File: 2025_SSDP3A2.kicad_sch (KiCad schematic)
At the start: 62 parts, among them J1 SolderPad, J2 SolderPad, J3 SolderPad, J4 SolderPad, J5 SolderPad_01x06, Q1 IAUZ30N10S5L240, Q2 BSZ096N10LS5, U1 LM5146RGYR

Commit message: Tweaks in schematic and layout
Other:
- note added: "V_{IN} = 20~60V (70V transient) typ. 6~12S Li-Ion/LiPo Battery"
- note removed: "V_{IN} = 20~70V (50V Nom) typ. 6~12S Li-Ion/LiPo Battery"
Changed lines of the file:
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@@
 		)
 	)
-	(text "V_{IN} = 20~70V (50V Nom)\ntyp. 6~12S Li-Ion/LiPo Battery"
+	(text "V_{IN} = 20~60V (70V transient)\ntyp. 6~12S Li-Ion/LiPo Battery"
 		(exclude_from_sim no)
 		(at 315.976 98.044 0)

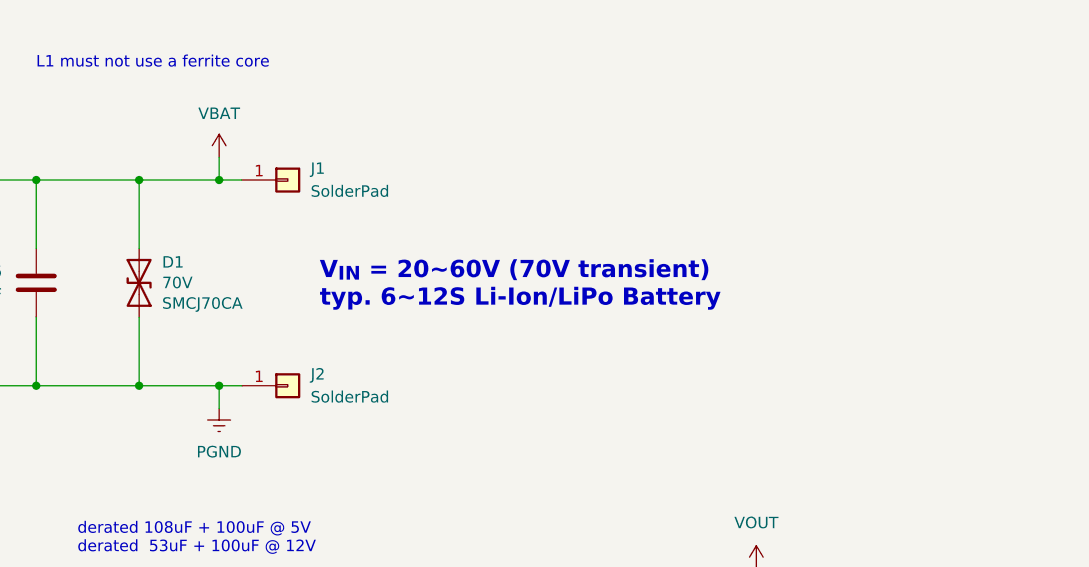
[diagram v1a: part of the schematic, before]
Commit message: Changed TVS diode
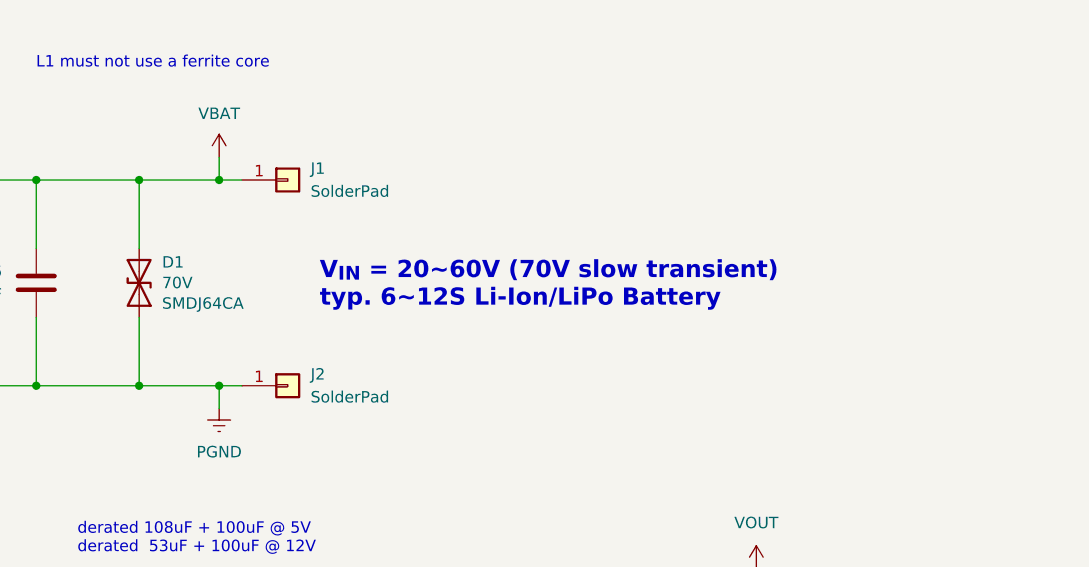
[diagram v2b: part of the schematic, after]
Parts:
- D1: LCSC PN C41411746 -> C42371551; Power (none) -> 3000W; Voltage 113V -> 103V
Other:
- note added: "V_{IN} = 20~60V (70V slow transient) typ. 6~12S Li-Ion/LiPo Battery"
- note removed: "V_{IN} = 20~60V (70V transient) typ. 6~12S Li-Ion/LiPo Battery"
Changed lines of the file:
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@@
 		)
 	)
-	(text "V_{IN} = 20~60V (70V transient)\ntyp. 6~12S Li-Ion/LiPo Battery"
+	(text "V_{IN} = 20~60V (70V slow transient)\ntyp. 6~12S Li-Ion/LiPo Battery"
 		(exclude_from_sim no)
 		(at 315.976 98.044 0)
@@
 			)
 		)
-		(property "Datasheet" "https://jlcpcb.com/api/file/downloadByFileSystemAccessId/8604441788598415360"
+		(property "Datasheet" "https://jlcpcb.com/api/file/downloadByFileSystemAccessId/8564879186138451968"
 			(at 295.91 97.79 0)
 			(effects
@@
 			)
 		)
-		(property "Description" "SMCJ70CA"
+		(property "Description" "SMDJ64CA"
 			(at 298.45 100.076 90)
 			(effects
@@
 			)
 		)
-		(property "LCSC PN" "C41411746"
+		(property "LCSC PN" "C42371551"
 			(at 295.91 97.79 90)
 			(effects
@@
 			)
 		)
-		(property "Voltage" "113V"
+		(property "Voltage" "103V"
 			(at 295.91 97.79 90)
 			(effects
@@
 			(at 295.91 97.79 90)
 			(effects
+				(font
+					(size 1.27 1.27)
+				)
+				(hide yes)
+			)
+		)
+		(property "Power" "3000W"
+			(at 295.91 97.79 90)
+			(effects

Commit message: Tweaks in schematic and layout
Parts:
- J5: now left out of the parts list
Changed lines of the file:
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@@
 		(unit 1)
 		(exclude_from_sim no)
-		(in_bom yes)
+		(in_bom no)
 		(on_board yes)
 		(dnp no)

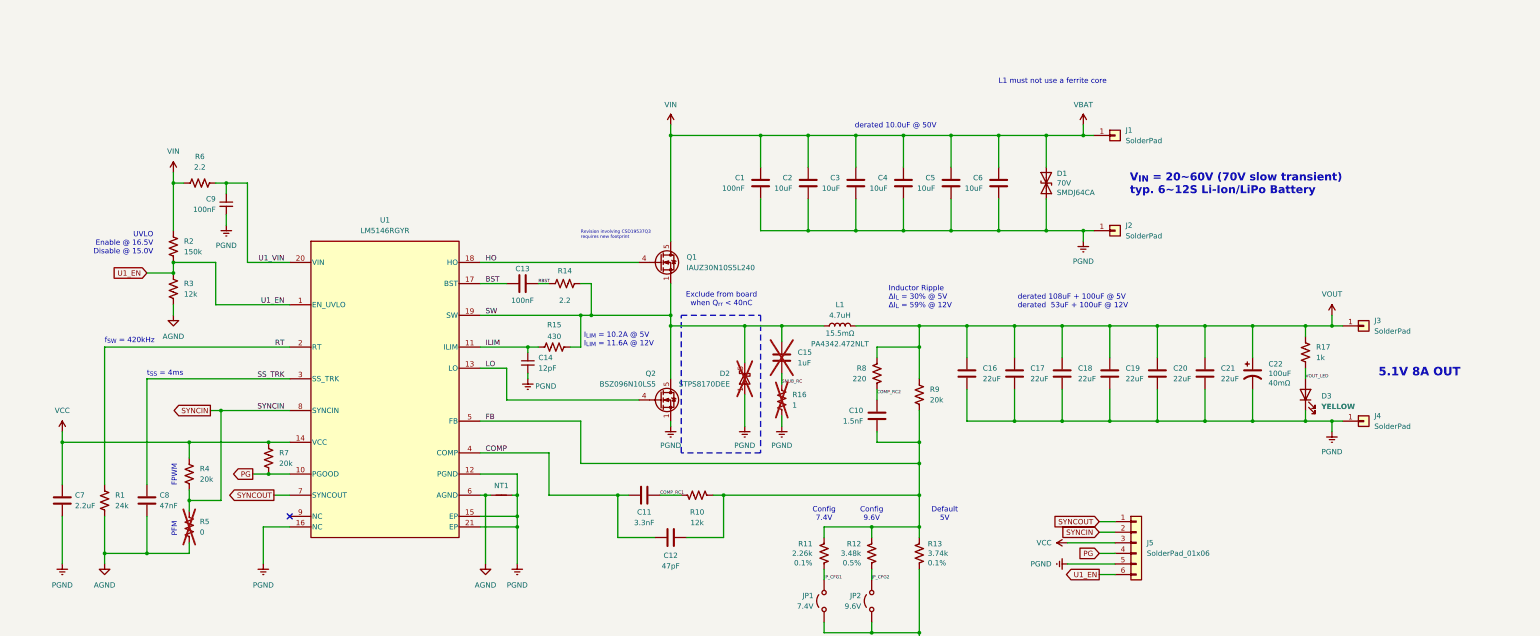
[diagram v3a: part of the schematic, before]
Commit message: Revised input TVS and added input cap
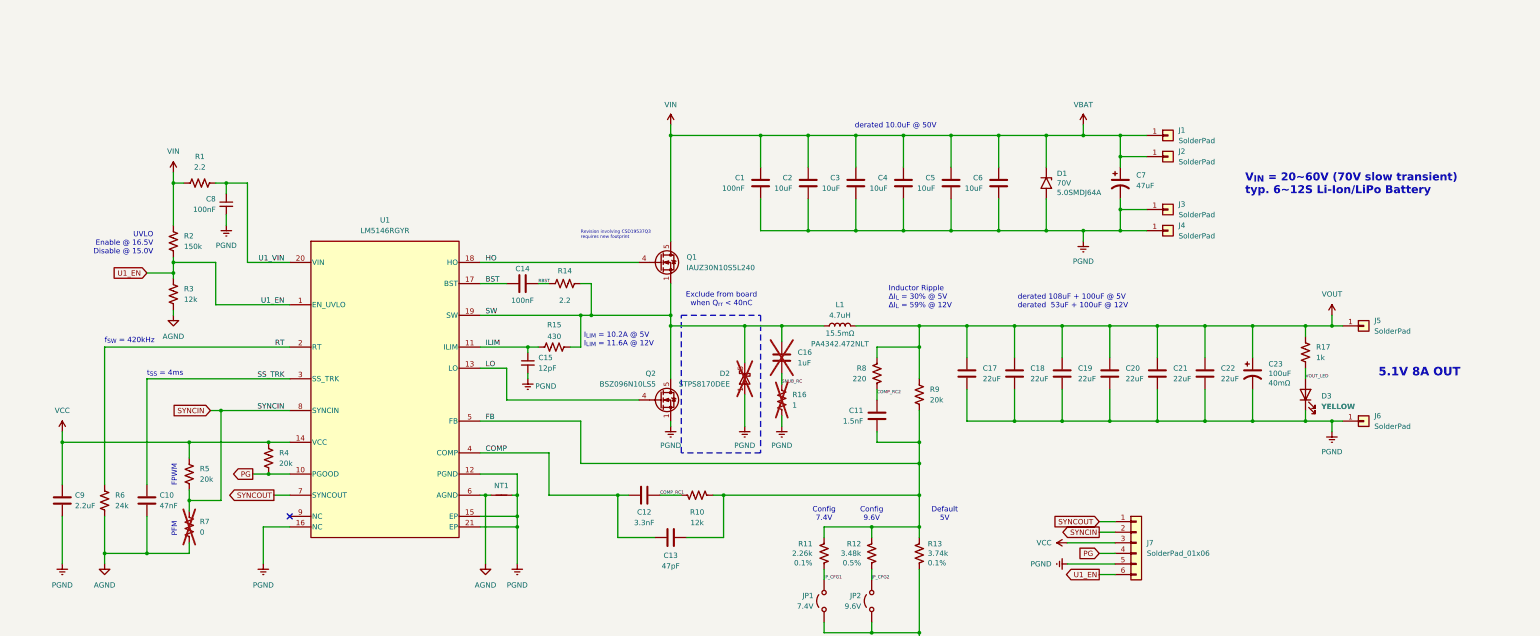
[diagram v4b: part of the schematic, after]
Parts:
- added C7: 47uF, symbol Device:C_Polarized_US
- added J2, J3: SolderPad, Connector_Wire:SolderWirePad_1x01_SMD_1.5x3mm, symbol Connector_Generic:Conn_01x01
- D1: symbol Diode:1.5SMCxxCA -> Diode:1.5SMCxxA; LCSC PN C42371551 -> C42394454; Part Type Preferred Extended -> Extended
- renumbered C8 to C10, C10 to C11, C11 to C12, C12 to C13, C13 to C14, C14 to C15, C15 to C16, C16 to C17, C17 to C18, C18 to C19, C19 to C20, C20 to C21, C21 to C22, C22 to C23, C9 to C8, C7 to C9, J2 to J4, J3 to J5, J4 to J6, J5 to J7, R6 to R1, R7 to R4, R4 to R5, R1 to R6, R5 to R7
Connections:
- net PGND: now also C7.2, J3.1 (Pin_1)
- net VBAT: now also C7.1, J2.1 (Pin_1)
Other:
- note removed: "L1 must not use a ferrite core"
- company: UBCO Aerospace Club -> UBCO Aerospace Club [Julian Joaquin]
- moved on the sheet: J1, J4, R2, R3

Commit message: Improvements to copper, added schematic notations
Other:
- note added: "Attach XT60-F connector via wires to pads"
- note added: "Attach XT60-M connector via wires to pads"
- moved on the sheet: C1, C10, C11, C12, C13, C14, C15, C16, C17, C18, C19, C2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
